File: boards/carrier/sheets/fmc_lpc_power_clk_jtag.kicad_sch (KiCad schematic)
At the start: 1 part, among them J4C FX10A-168P-SV(91)

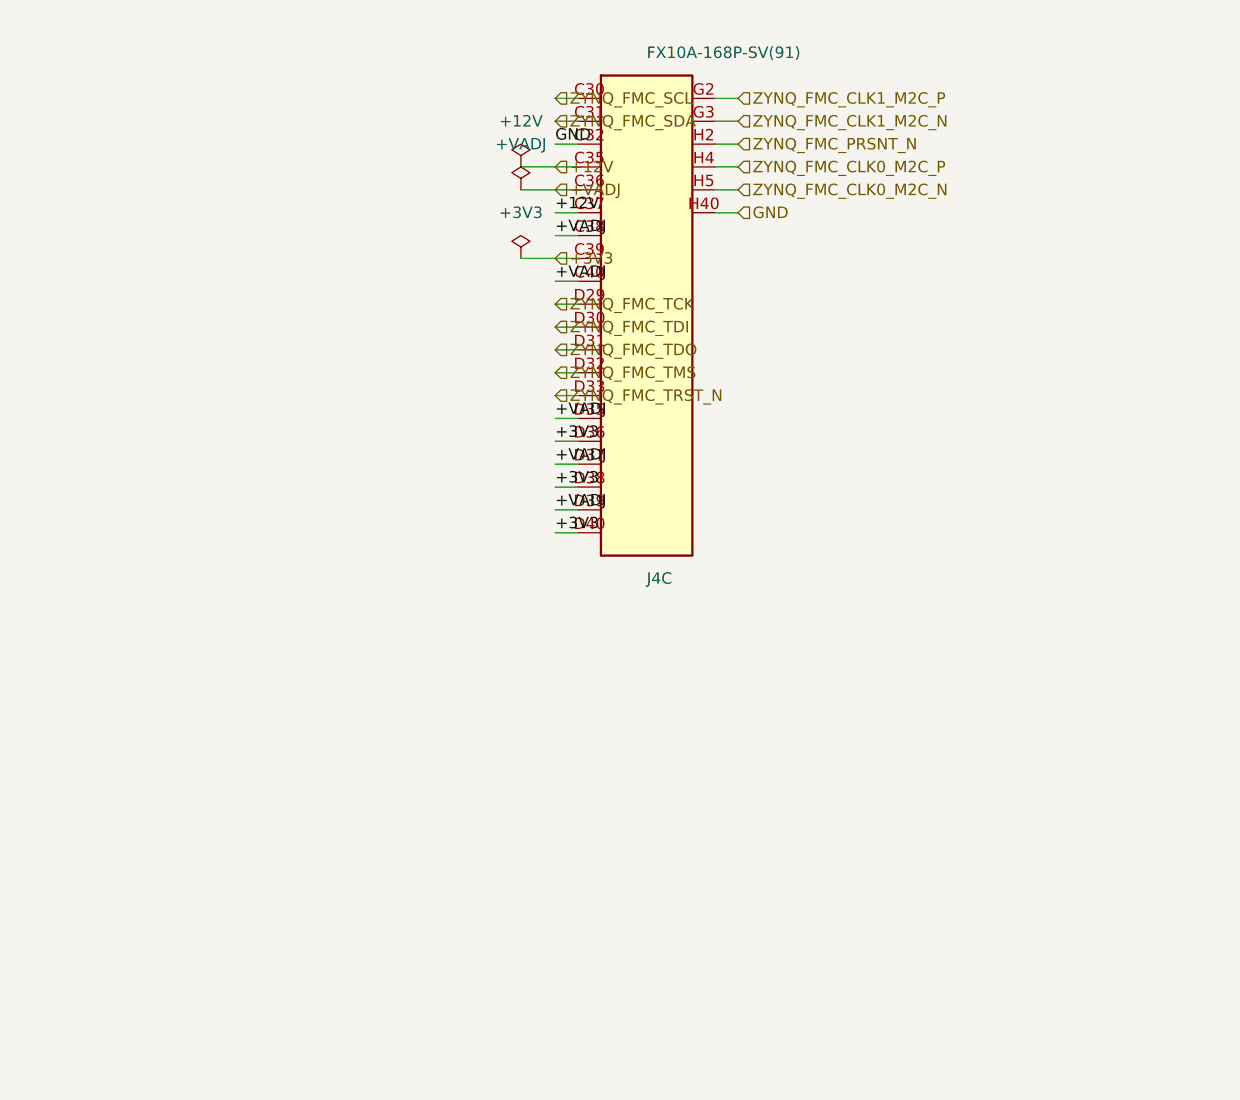
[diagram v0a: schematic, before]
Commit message: symbols+placement: intrinsic-text-aware layout (no hiding)
Wave D Steps 0-3 (revert + intrinsic bbox infra + validator extension):

Step 0 — Reverted pin_names hiding I added earlier:
* zynq_eda.kicad_sym: stripped (pin_names (hide yes)) from USBC_16P,
  FFC_40P, FFC_15P, JTAG_2x7, SWD_2x5, HX5008NLT, RJHSE5380, SW_DIP_4.
* connector_bank_symbols: restored show_pin_names=True.
* All 14 auto-generated bank symbols regenerated with names visible.

Step 1 — Intrinsic text bbox helpers (core/layout/geometry.py):
* New SymbolGeometryCache.intrinsic_pin_label_bboxes() and
  intrinsic_pin_number_bboxes() — return PAGE-coord bboxes for the
  pin-NAME and pin-NUMBER text KiCad paints from the .kicad_sym
  definition. Parses the symbol's (pin_names (offset N) (hide)) and
  (pin_numbers (hide)) directives.
* New BBoxKind values "intrinsic_pin_name" and "intrinsic_pin_number"
  in core/layout/bbox.py.

Step 2 — Occupancy registers intrinsic bboxes (core/layout/_builder.py):
* BlockLayoutBuilder.add_symbol now also registers every intrinsic
  pin-name + pin-number bbox so the live spatial index sees them.
  Subsequent placement consults find_free_offset and can avoid them.

Step 3 — Validator extension (core/validate/overlap.py):
* New checks: label × intrinsic_pin_name, label × intrinsic_pin_number,
  hlabel × intrinsic_pin_name, hlabel × intrinsic_pin_number.
* Exempts labels anchored at the symbol's own pin endpoints
  (legitimate "net label attached to pin's intrinsic name" pattern).

Symbol-side fixes (the visual win):
* connector_banks.py generator: pin pitch 2.54 → 5.08 mm, body
  half-width 5.08 → 12.7 mm. Bank symbols now have 5 mm clear gap
  between rows — pin names readable without overlapping numbers.
* zynq_eda.kicad_sym: doubled pin Y coords on USBC_16P, FFC_40P,
  FFC_15P, HX5008NLT, RJHSE5380 (115 y-coord substitutions). All
  now at 5.08 mm pin pitch, matching the bank convention.

State:
* 0 ERC errors. 0 overlap warnings.
* USB-C OTG page (was unreadable per 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
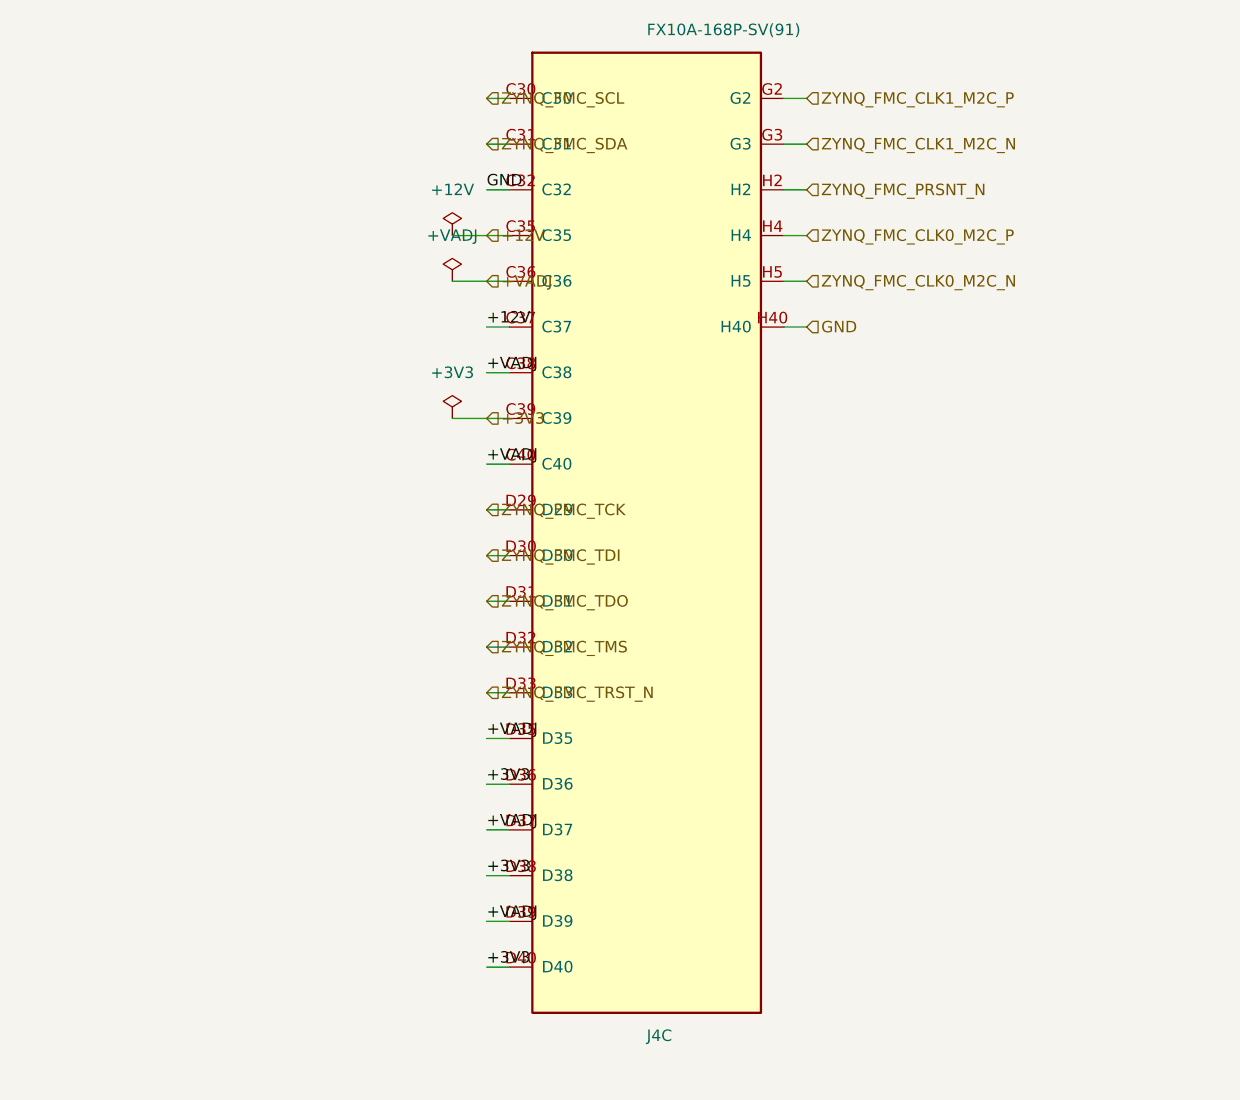
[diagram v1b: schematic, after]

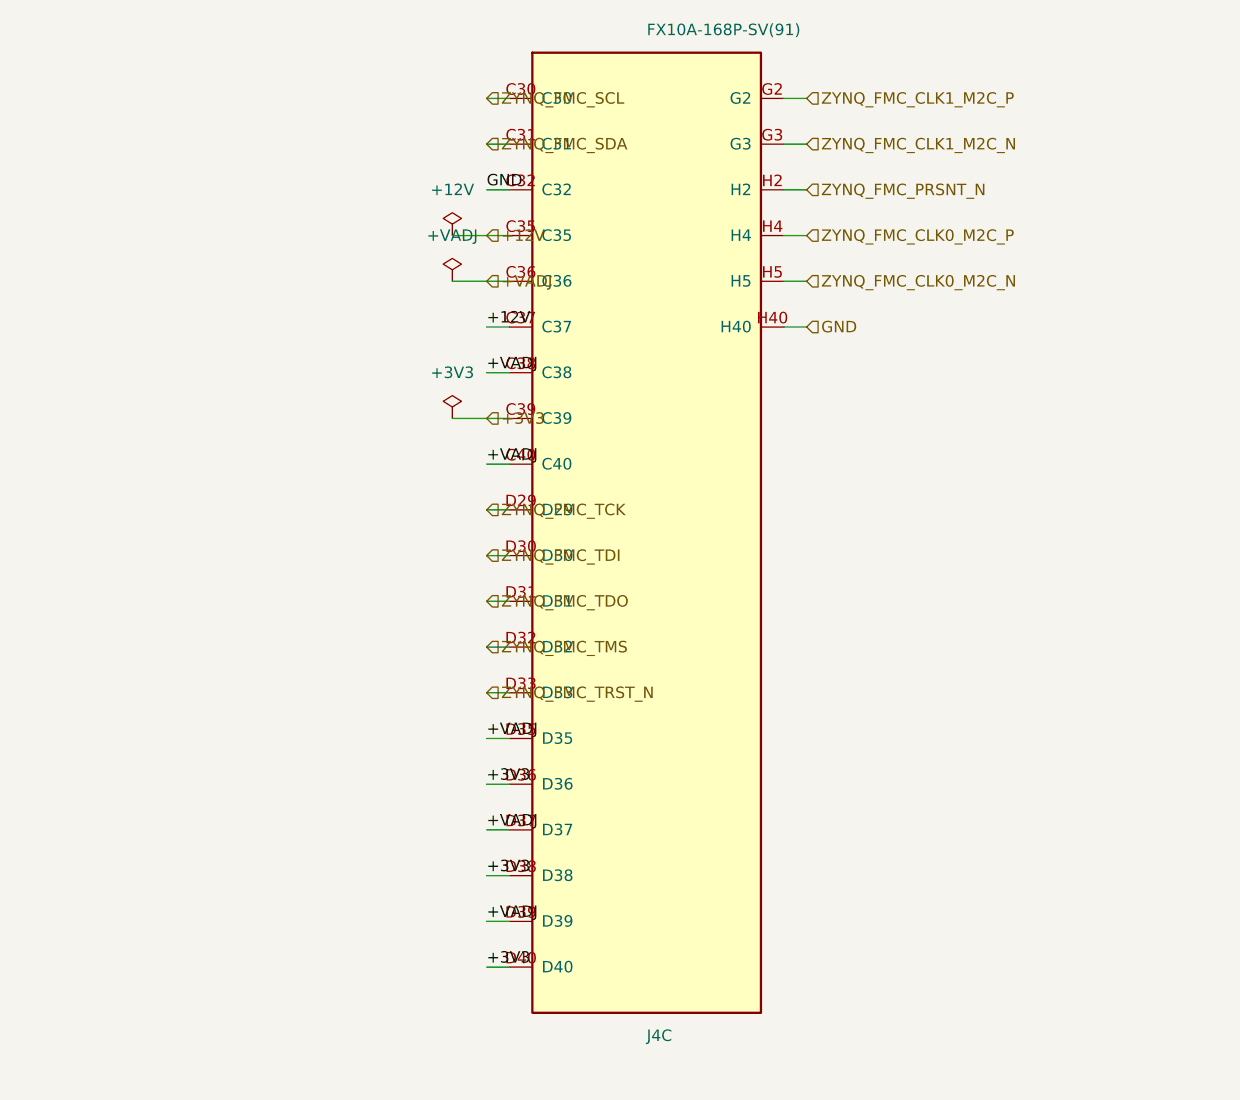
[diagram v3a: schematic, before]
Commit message: layout: no-stub connectors + bbox-based page-bounds + longer pin length
Three changes informed by user iteration:

1. STUB_LEN dropped (connectors.py): our PlacedLabels now anchor
   DIRECTLY at the connector pin tip — no extra stub wire. The
   symbol's intrinsic pin LINE (the 2.54-5.08 mm pin stub drawn by
   the symbol itself) is the only separation between body and label.
   User directive: "no fucking stubbs ever".

2. Bank-symbol pin length doubled (connector_banks.py): pins now
   render with length=5.08 mm (was 2.54 default). Gives the
   intrinsic pin-number text ~5 mm of horizontal room in the stub
   area instead of ~2.5 mm, so pin number text doesn't crowd
   adjacent text bboxes.

3. validate/page_bounds.py rewritten to bbox-based: every
   primitive's FULL bbox must lie inside the margin (was anchor-
   point check, missed labels with anchor on-page but text
   extending off-page). Covers symbol bodies, wires, local labels,
   hier labels, global labels, sub-sheet rectangles, junctions,
   no-connects. User rule: "all wires, label symbols must
   absolutely must be within page bounds".

4. Text width bbox ratio bumped 0.6 → 0.85 (bbox.py): KiCad's
   stroke font is closer to 0.85× height per char than 0.6×; the
   conservative over-estimate catches near-misses better.

5. New core/layout/template.py (Wave F context): the single source
   of truth for shared layout attributes (pin pitch, text size,
   body proportions, stub length, cap-chain clearance). Documented
   the carrier's "no hiding, no overlap, in-bounds" rules.

State: 0 bounds errors. 4 overlap errors remain (the CP2102N
+3V3 rail crossing pin names — to be fixed by Steiner-tree
multi-pin routing in Phase F1/F2, not yet implemented).

Co-Authored-By: Claude Opus 4.7 (1M context) <noreply@anthropic.com>
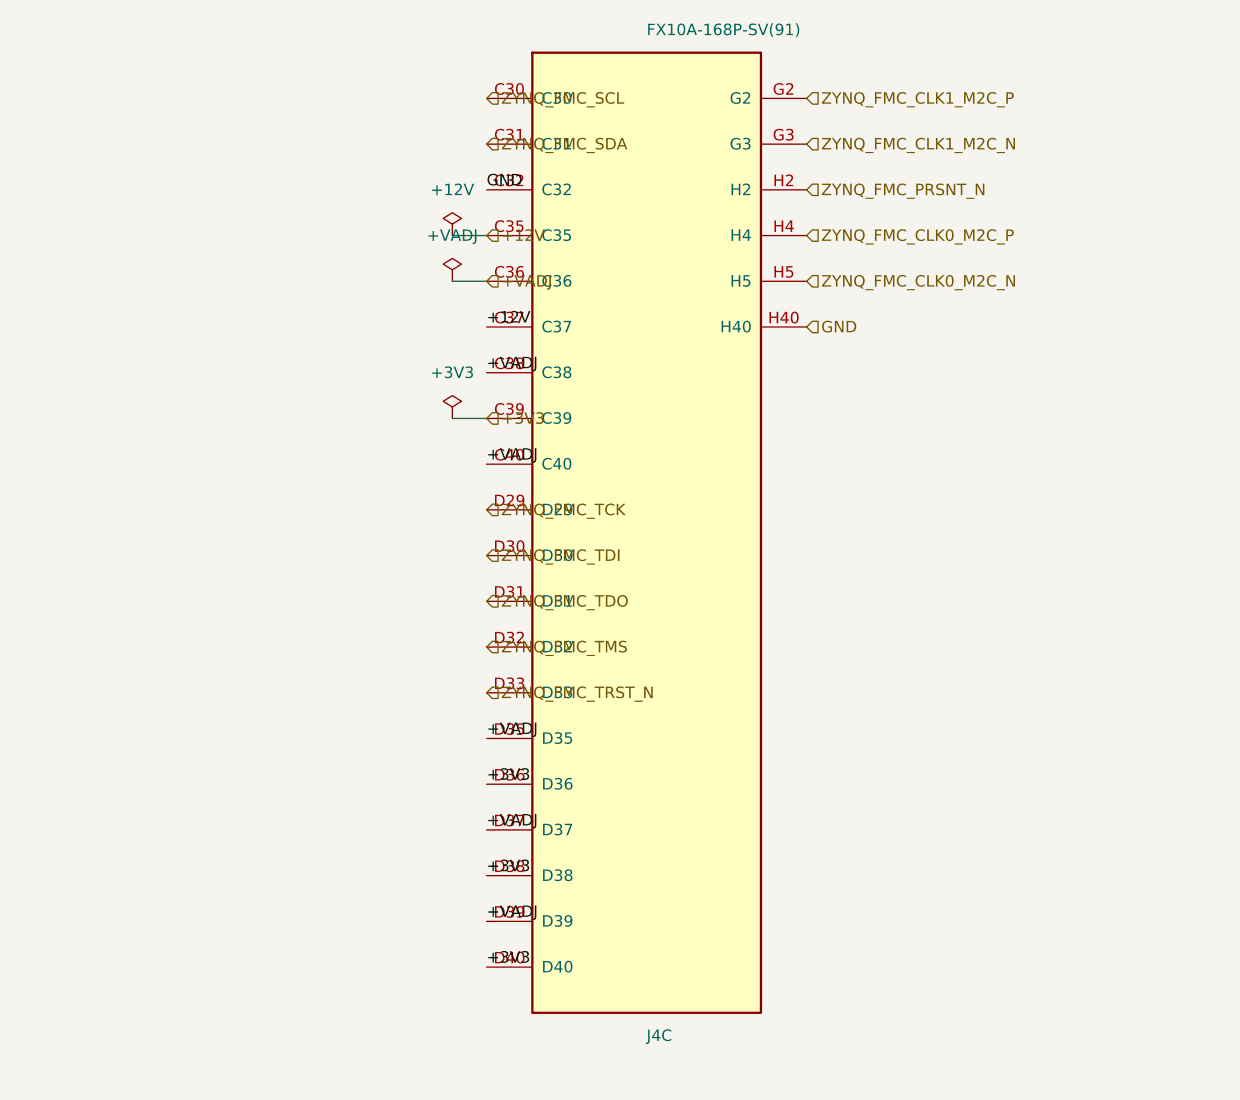
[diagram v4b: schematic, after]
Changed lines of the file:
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@@
 		(instances
 			(project "FMC LPC bank C (power + clock + JTAG + mgmt)"
-				(path "/b063a2c8-43d8-4f2e-b19c-6bb15d22c92c"
+				(path "/913db5c8-e5dd-43f9-89a7-563d0f10e47d"
 					(reference "J4C")
 					(unit 1)
@@
 		(instances
 			(project "FMC LPC bank C (power + clock + JTAG + mgmt)"
-				(path "/b063a2c8-43d8-4f2e-b19c-6bb15d22c92c"
+				(path "/913db5c8-e5dd-43f9-89a7-563d0f10e47d"
 					(reference "#FLG100")
 					(unit 1)
@@
 		(instances
 			(project "FMC LPC bank C (power + clock + JTAG + mgmt)"
-				(path "/b063a2c8-43d8-4f2e-b19c-6bb15d22c92c"
+				(path "/913db5c8-e5dd-43f9-89a7-563d0f10e47d"
 					(reference "#FLG101")
 					(unit 1)
@@
 		(instances
 			(project "FMC LPC bank C (power + clock + JTAG + mgmt)"
-				(path "/b063a2c8-43d8-4f2e-b19c-6bb15d22c92c"
+				(path "/913db5c8-e5dd-43f9-89a7-563d0f10e47d"
 					(reference "#FLG102")
 					(unit 1)
@@
 	(wire
 		(pts
-			(xy 322.58 52.07) (xy 328.93 52.07)
+			(xy 322.58 52.07) (xy 326.39 52.07)
 		)
 		(stroke
@@
 	(wire
 		(pts
-			(xy 359.41 52.07) (xy 361.95 52.07)
+			(xy 322.58 72.39) (xy 326.39 72.39)
 		)
 		(stroke
@@
 	(wire
 		(pts
-			(xy 322.58 57.15) (xy 328.93 57.15)
+			(xy 322.58 57.15) (xy 326.39 57.15)
 		)
 		(stroke
-			(width 0)
-			(type default)
-		)
-	)
-	(wire
-		(pts
-			(xy 359.41 57.15) (xy 361.95 57.15)
-		)
-		(stroke
-			(width 0)
-			(type default)
-		)
-	)
-	(wire
-		(pts
-			(xy 326.39 36.83) (xy 328.93 36.83)
-		)
-		(stroke
-			(width 0)
-			(type default)
-		)
-	)
-	(wire
-		(pts
-			(xy 359.41 36.83) (xy 361.95 36.83)
-		)
-		(stroke
-			(width 0)
-			(type default)
-		)
-	)
-	(wire
-		(pts
-			(xy 326.39 41.91) (xy 328.93 41.91)
-		)
-		(stroke
-			(width 0)
-			(type default)
-		)
-	)
-	(wire
-		(pts
-			(xy 359.41 41.91) (xy 361.95 41.91)
-		)
-		(stroke
-			(width 0)
-			(type default)
-		)
-	)
-	(wire
-		(pts
-			(xy 326.39 82.55) (xy 328.93 82.55)
-		)
-		(stroke
-			(width 0)
-			(type default)
-		)
-	)
-	(wire
-		(pts
-			(xy 326.39 87.63) (xy 328.93 87.63)
-		)
-		(stroke
-			(width 0)
-			(type default)
-		)
-	)
-	(wire
-		(pts
-			(xy 326.39 92.71) (xy 328.93 92.71)
-		)
-		(stroke
-			(width 0)
-			(type default)
-		)
-	)
-	(wire
-		(pts
-			(xy 326.39 97.79) (xy 328.93 97.79)
-		)
-		(stroke
-			(width 0)
-			(type default)
-		)
-	)
-	(wire
-		(pts
-			(xy 326.39 102.87) (xy 328.93 102.87)
-		)
-		(stroke
-			(width 0)
-			(type default)
-		)
-	)
-	(wire
-		(pts
-			(xy 326.39 46.99) (xy 328.93 46.99)
-		)
-		(stroke
-			(width 0)
-			(type default)
-		)
-	)
-	(wire
-		(pts
-			(xy 359.41 46.99) (xy 361.95 46.99)
-		)
-		(stroke
-			(width 0)
-			(type default)
-		)
-	)
-	(wire
-		(pts
-			(xy 326.39 62.23) (xy 328.93 62.23)
-		)
-		(stroke
-			(width 0)
-			(type default)
-		)
-	)
-	(wire
-		(pts
-			(xy 359.41 62.23) (xy 361.95 62.23)
-		)
-		(stroke
-			(width 0)
-			(type default)
-		)
-	)
-	(wire
-		(pts
-			(xy 322.58 72.39) (xy 328.93 72.39)
-		)
-		(stroke
-			(width 0)
-			(type default)
-		)
-	)
-	(wire
-		(pts
-			(xy 326.39 113.03) (xy 328.93 113.03)
-		)
-		(stroke
-			(width 0)
-			(type default)
-		)
-	)
-	(wire
-		(pts
-			(xy 326.39 123.19) (xy 328.93 123.19)
-		)
-		(stroke
-			(width 0)
-			(type default)
-		)
-	)
-	(wire
-		(pts
-			(xy 326.39 133.35) (xy 328.93 133.35)
-		)
-		(stroke
-			(width 0)
-			(type default)
-		)
-	)
-	(wire
-		(pts
-			(xy 326.39 67.31) (xy 328.93 67.31)
-		)
-		(stroke
-			(width 0)
-			(type default)
-		)
-	)
-	(wire
-		(pts
-			(xy 326.39 77.47) (xy 328.93 77.47)
-		)
-		(stroke
-			(width 0)
-			(type default)
-		)
-	)
-	(wire
-		(pts
-			(xy 326.39 107.95) (xy 328.93 107.95)
-		)
-		(stroke
-			(width 0)
-			(type default)
-		)
-	)
-	(wire
-		(pts
-			(xy 326.39 118.11) (xy 328.93 118.11)
-		)
-		(stroke
-			(width 0)
-			(type default)
-		)
-	)
-	(wire
-		(pts
-			(xy 326.39 128.27) (xy 328.93 128.27)
-		)
-		(stroke

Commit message: boards/carrier: regenerate with predictive planner (27/27 clean)
All 27 sheet .kicad_sch files regenerated by the planner with
bounds=0, overlap=0 per block. Includes updated validation_report.md
(zero layout errors; only ERC pin_not_connected for unused IC pins),
audit_report.md, BOM, IO assignment, reference circuits, and root
sheet / project file.

Co-Authored-By: Claude Opus 4.7 <noreply@anthropic.com>
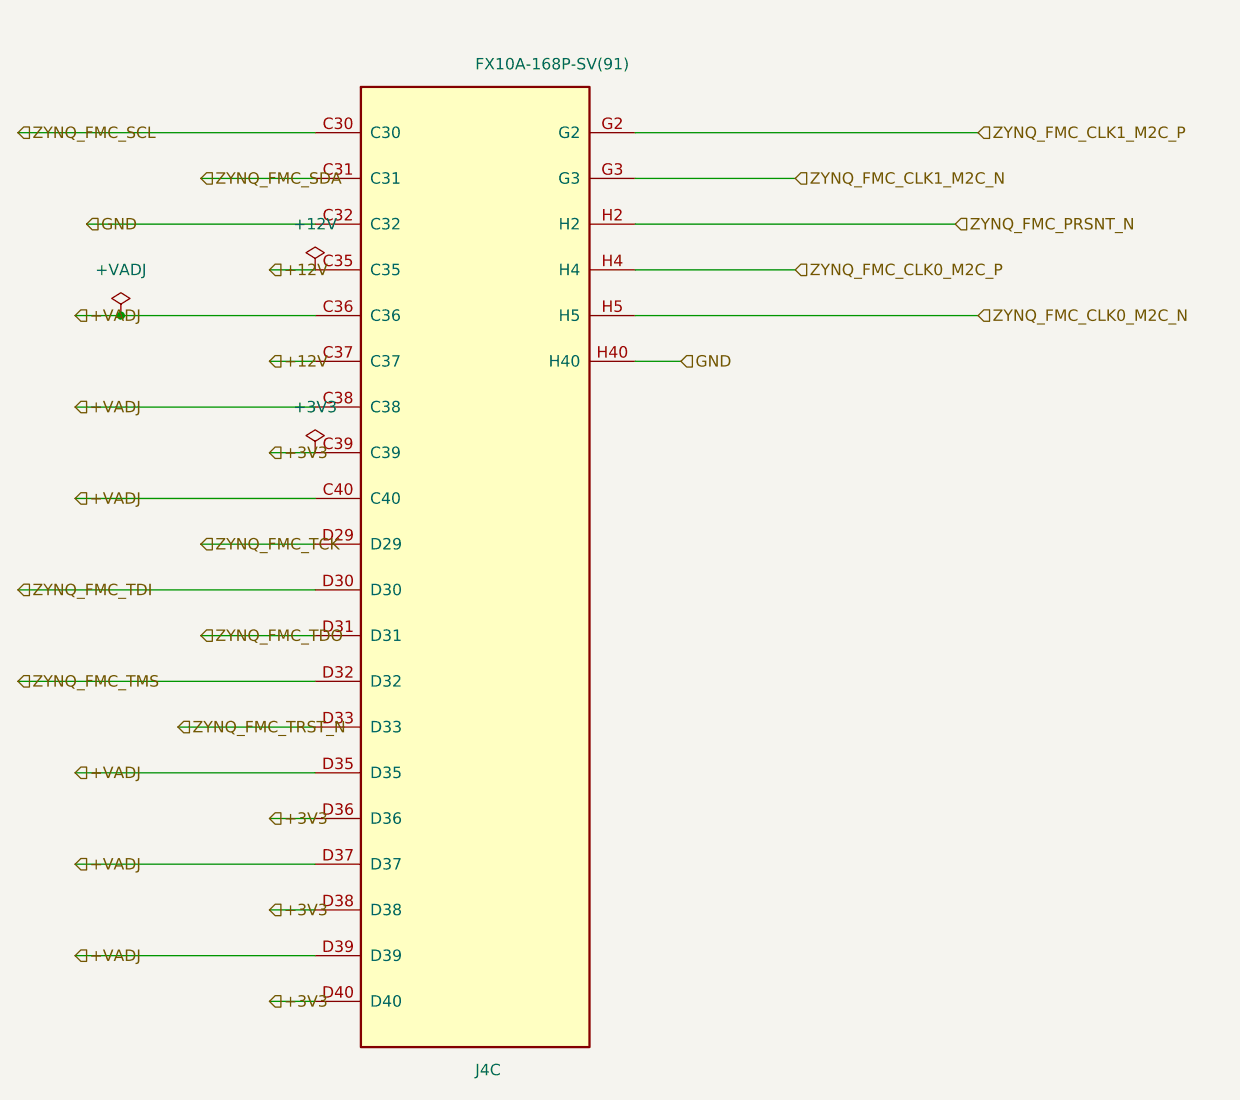
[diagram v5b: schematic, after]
